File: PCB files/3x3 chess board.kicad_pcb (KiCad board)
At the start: 2 copper layers, 189 x 115.1 mm, 81 parts, among them J1 Conn_01x03, J10 Conn_01x02, J11 USB4216-03-A_REVA, J12 Conn_01x03, J2 Conn_01x03, J4 Conn_01x03, J5 Conn_01x03, J6 Conn_01x03, J7 Conn_01x03, J8 Conn_01x03, J9 Conn_01x03, U1 MCP23S17_SO, U2 MCP23S17_SO, U3 W25Q128JVS, U4 RP2040, X1 ABM8-272-T3

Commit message: update
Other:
- board size 189 x 115.1 mm -> 125.3 x 114.6 mm
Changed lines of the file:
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@@
 	(gr_line
 		(start 49.74 44.25)
-		(end 238.77 43.53)
+		(end 175.04 43.84)
 		(stroke
 			(width 0.05)
@@
 	)
 	(gr_line
-		(start 237.78 158.62)
+		(start 174.864772 158.48945)
 		(end 49.83 158.23)
 		(stroke
@@
 		(polygon
 			(pts
-				(xy 49 47) (xy 49 160) (xy 237 160) (xy 238.032967 158.967033) (xy 238.032967 45) (xy 51 45)
+				(xy 49 47) (xy 49 160) (xy 174.56 159.18) (xy 175.582967 159.204287) (xy 175.582967 45) (xy 51 45)
 			)
 		)
@@
 		(polygon
 			(pts
-				(xy 238 157) (xy 49 161) (xy 49 45) (xy 239 45) (xy 239 41) (xy 239 46)
+				(xy 175.58 158.77) (xy 49 161) (xy 49 45) (xy 174.26 45.06) (xy 174.86 45.36) (xy 175.35 45.18)
 			)
 		)

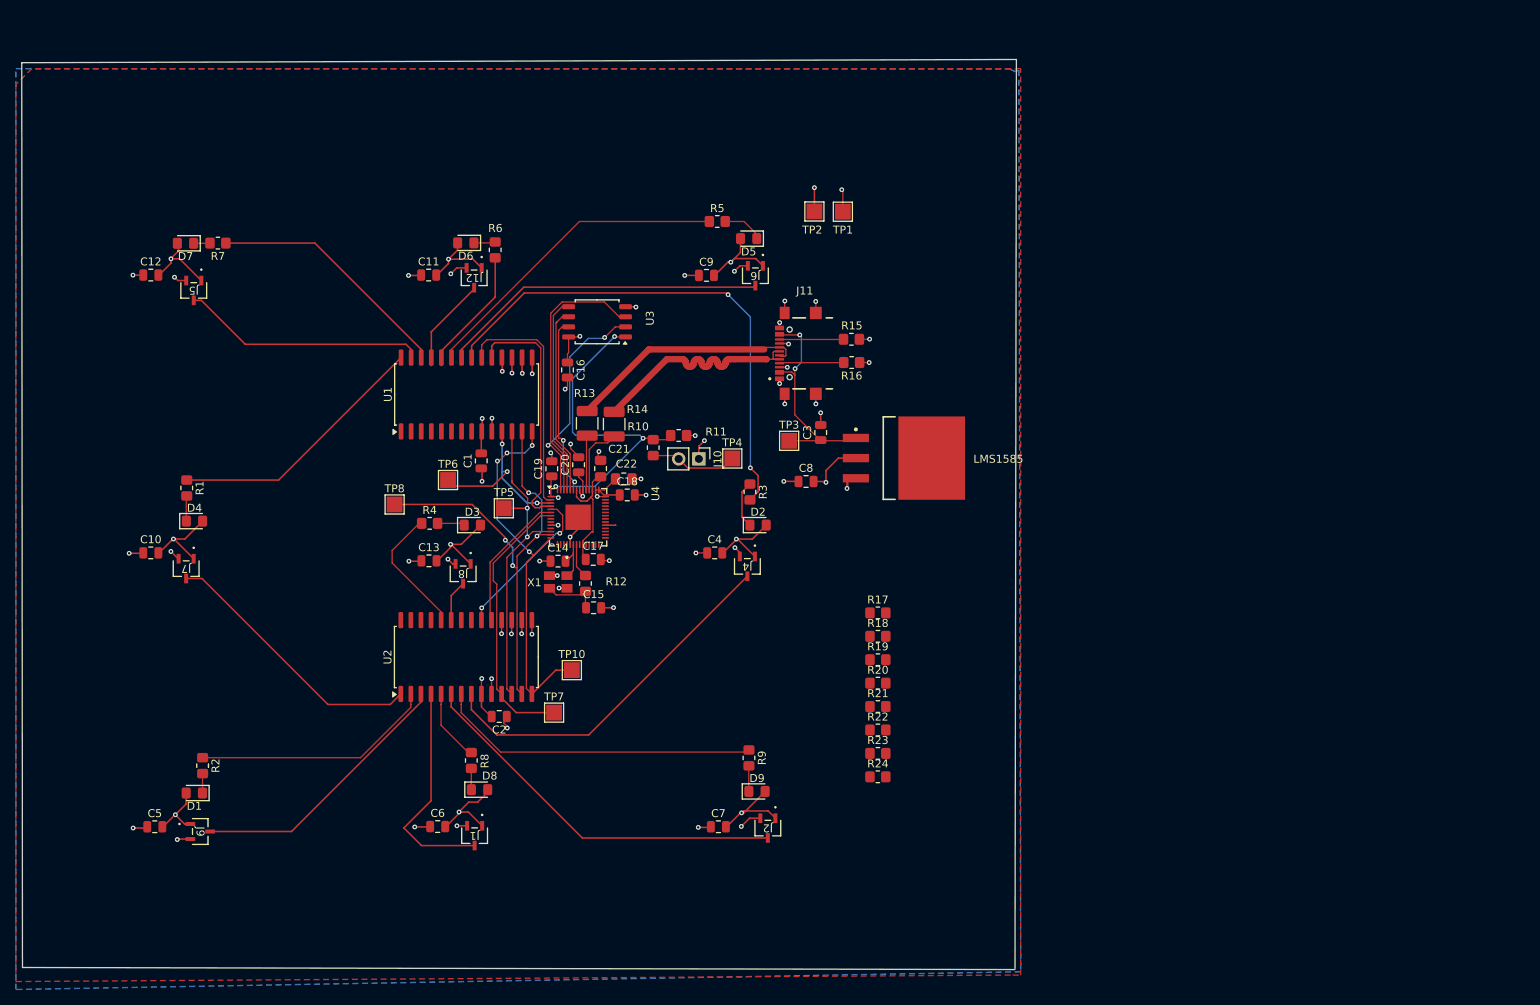
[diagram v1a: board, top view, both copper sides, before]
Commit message: update schematic and and pcb w/ new mcu
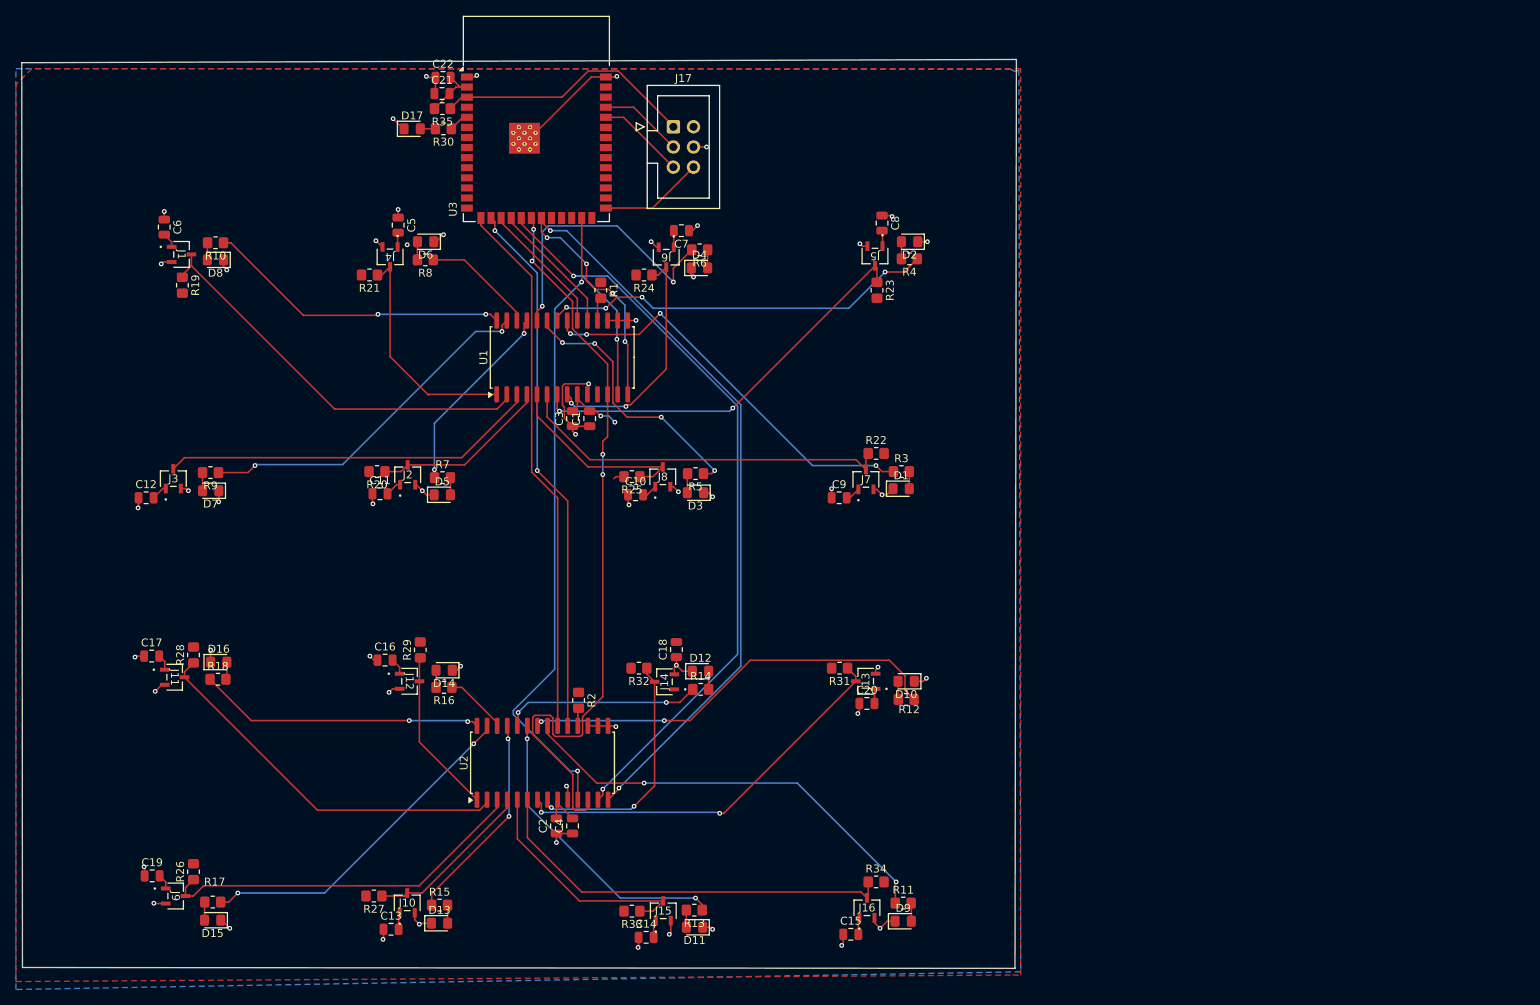
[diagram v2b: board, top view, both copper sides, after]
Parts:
- removed LMS1585: ~, LMS1585:KTT0003B
- removed TP1, TP10, TP3, TP4, TP5, TP6, TP7, TP8: TestPoint, TestPoint:TestPoint_Pad_2.0x2.0mm
- removed TP2: Ground test point, TestPoint:TestPoint_Pad_2.0x2.0mm
- removed U4: RP2040, Package_DFN_QFN:QFN-56-1EP_7x7mm_P0.4mm_EP3.2x3.2mm
- removed X1: ABM8-272-T3, ABM8 - 272 - T3:ABM8-272-T3_ABR
- added D10: LED, Diode_SMD:D_0805_2012Metric_Pad1.15x1.40mm_HandSolder, F.Cu at (161.2, 122.2)
- added D11: LED, Diode_SMD:D_0805_2012Metric_Pad1.15x1.40mm_HandSolder, F.Cu at (134.5, 153.2)
- added D12: LED, Diode_SMD:D_0805_2012Metric_Pad1.15x1.40mm_HandSolder, F.Cu at (135.2, 120.9)
- added D13: LED, Diode_SMD:D_0805_2012Metric_Pad1.15x1.40mm_HandSolder, F.Cu at (102.4, 152.7)
- added D14: LED, Diode_SMD:D_0805_2012Metric_Pad1.15x1.40mm_HandSolder, F.Cu at (103.0, 120.8)
- added D15: LED, Diode_SMD:D_0805_2012Metric_Pad1.15x1.40mm_HandSolder, F.Cu at (73.8, 152.3)
- added D16: LED, Diode_SMD:D_0805_2012Metric_Pad1.15x1.40mm_HandSolder, F.Cu at (74.6, 119.8)
- added D17: LED, Diode_SMD:D_0805_2012Metric_Pad1.15x1.40mm_HandSolder, F.Cu at (98.9, 52.6)
- added J13: Conn_01x03, Hall effect sensor:TSOT-3L_MLX92232LSE-AAA-002-SP_MEL, F.Cu at (156.1, 122.2)
- added J14: Conn_01x03, Hall effect sensor:TSOT-3L_MLX92232LSE-AAA-002-SP_MEL, F.Cu at (130.7, 122.2)
- added J15: Conn_01x03, Hall effect sensor:TSOT-3L_MLX92232LSE-AAA-002-SP_MEL, F.Cu at (130.6, 151.1)
- added J16: Conn_01x03, Hall effect sensor:TSOT-3L_MLX92232LSE-AAA-002-SP_MEL, F.Cu at (156.2, 150.7)
- added J17: Conn_02x03_Odd_Even, Connector_IDC:IDC-Header_2x03_P2.54mm_Vertical, F.Cu at (131.8, 52.3)
- added J3: Conn_01x03, Hall effect sensor:TSOT-3L_MLX92232LSE-AAA-002-SP_MEL, F.Cu at (68.8, 96.6)
- added R25: 5k, Resistor_SMD:R_0805_2012Metric_Pad1.20x1.40mm_HandSolder, F.Cu at (126.6, 96.4)
- added R26: 5k, Resistor_SMD:R_0805_2012Metric_Pad1.20x1.40mm_HandSolder, F.Cu at (71.4, 146.2)
- added R27: 5k, Resistor_SMD:R_0805_2012Metric_Pad1.20x1.40mm_HandSolder, F.Cu at (94.1, 149.2)
- added R28: 5k, Resistor_SMD:R_0805_2012Metric_Pad1.20x1.40mm_HandSolder, F.Cu at (71.4, 118.9)
- added R29: 5k, Resistor_SMD:R_0805_2012Metric_Pad1.20x1.40mm_HandSolder, F.Cu at (99.9, 118.2)
- added R30: 320, Resistor_SMD:R_0805_2012Metric_Pad1.20x1.40mm_HandSolder, F.Cu at (102.9, 52.6)
- added R31: 5k, Resistor_SMD:R_0805_2012Metric_Pad1.20x1.40mm_HandSolder, F.Cu at (152.8, 120.5)
- added R32: 5k, Resistor_SMD:R_0805_2012Metric_Pad1.20x1.40mm_HandSolder, F.Cu at (127.5, 120.5)
- added R33: 5k, Resistor_SMD:R_0805_2012Metric_Pad1.20x1.40mm_HandSolder, F.Cu at (126.6, 151.1)
- added R34: 5k, Resistor_SMD:R_0805_2012Metric_Pad1.20x1.40mm_HandSolder, F.Cu at (157.4, 147.4)
- added R35: 5k, Resistor_SMD:R_0805_2012Metric_Pad1.20x1.40mm_HandSolder, F.Cu at (102.7, 50.0)
- C14, C15: value 15pF -> 10nF
- C16, C17, C18, C19, C20: value 0.1uF -> 10nF
- C21: footprint Capacitor_SMD:C_0805_2012Metric_Pad1.18x1.45mm_HandSolder -> Capacitor_SMD:C_0805_2012Metric
- C22: value 1uF -> 0.1uF; footprint Capacitor_SMD:C_0805_2012Metric_Pad1.18x1.45mm_HandSolder -> Capacitor_SMD:C_0805_2012Metric
- C3: value 10uF -> 1uF
- C4: value 10nF -> 1uF
- C8: value 10uF -> 10nF
- J10: value Conn_01x02 -> Conn_01x03; footprint Connector_PinHeader_2.54mm:PinHeader_1x02_P2.54mm_Vertical -> Hall effect sensor:TSOT-3L_MLX92232LSE-AAA-002-SP_MEL
- J11: value USB4216-03-A_REVA -> Conn_01x03; footprint USB receptacle:USB 2.0 -> Hall effect sensor:TSOT-3L_MLX92232LSE-AAA-002-SP_MEL
- R1, R2: value 16 -> 5k
- R10, R12: value 1k -> 16
- R11: value do not fit -> 16
- R13, R14: value 27.4 -> 16; footprint Resistor_SMD:R_1210_3225Metric_Pad1.30x2.65mm_HandSolder -> Resistor_SMD:R_0805_2012Metric_Pad1.20x1.40mm_HandSolder
- R15, R16: value 5.1kΩ -> 16
- R17, R18: value 5k -> 16
- U3: value W25Q128JVS -> ESP32-S3-WROOM-1; footprint Package_SO:SOIC-8_5.3x5.3mm_P1.27mm -> RF_Module:ESP32-S3-WROOM-1
- moved R19 99.5 mm to (70.0, 72.3), turned to -90 degrees
- moved D1 96.9 mm to (160.5, 97.9), turned to 0 degrees
- moved R17 91.4 mm to (73.8, 150.0), turned to 180 degrees
- moved J11 89.5 mm to (69.0, 121.7), turned to -90 degrees
- moved J7 86.4 mm to (156.1, 96.8), turned to 0 degrees
- moved J5 85.9 mm to (157.2, 68.6)
- moved R15 85.8 mm to (102.4, 150.4)
- moved R21 84.0 mm to (93.5, 71.0), turned to 180 degrees
- moved R18 83.3 mm to (74.5, 121.9)
- moved C6 83.0 mm to (67.7, 65.0), turned to -90 degrees
- moved J1 82.0 mm to (69.9, 68.4), turned to -90 degrees
- moved C5 81.8 mm to (97.2, 64.7), turned to -90 degrees
- moved R9 76.8 mm to (73.5, 95.9), turned to 180 degrees
- moved C7 75.2 mm to (132.8, 65.4), turned to 180 degrees
- moved D8 74.6 mm to (74.1, 69.1), turned to 180 degrees
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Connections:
- C14 pad 2: /XIN -> +3.3V
- C15 pad 1: Net-(C15-Pad1) -> GND
- C15 pad 2: GND -> +3.3V
- C16 pad 1: +3.3V -> GND
- C16 pad 2: GND -> +3.3V
- C17 pad 1: +1V1 -> GND
- C17 pad 2: GND -> +3.3V
- C18 pad 1: +3.3V -> GND
- C18 pad 2: GND -> +3.3V
- C19 pad 1: +3.3V -> GND
- C19 pad 2: GND -> +3.3V
- C20 pad 1: +3.3V -> GND
- C20 pad 2: GND -> +3.3V
- C21 pad 1: +1V1 -> GND
- C21 pad 2: GND -> +3.3V
- C22 pad 1: +3.3V -> GND
- C22 pad 2: GND -> +3.3V
- C3 pad 1: VBUS -> GND
- C3 pad 2: GND -> +3.3V
- C8 pad 1: +3.3V -> GND
- C8 pad 2: GND -> +3.3V
- D1 pad 1: Net-(D1-K) -> GND
- D1 pad 2: +3.3V -> Net-(D1-A)
- D2 pad 1: Net-(D2-K) -> GND
- D2 pad 2: +3.3V -> Net-(D2-A)
- D3 pad 1: Net-(D3-K) -> GND
- D3 pad 2: +3.3V -> Net-(D3-A)
- D4 pad 1: Net-(D4-K) -> GND
- D4 pad 2: +3.3V -> Net-(D4-A)
- D5 pad 1: Net-(D5-K) -> GND
- D5 pad 2: +3.3V -> Net-(D5-A)
- D6 pad 1: Net-(D6-K) -> GND
- D6 pad 2: +3.3V -> Net-(D6-A)
- D7 pad 1: Net-(D7-K) -> GND
- D7 pad 2: +3.3V -> Net-(D7-A)
- D8 pad 1: Net-(D8-K) -> GND
- D8 pad 2: +3.3V -> Net-(D8-A)
- D9 pad 1: Net-(D9-K) -> GND
- D9 pad 2: +3.3V -> Net-(D9-A)
- J1 pad 3: /HALL8 -> /HALL2
- J10 pad 1: GND -> +3.3V
- J10 pad 2: Net-(J10-Pin_2) -> GND
- J12 pad 3: /HALL1 -> /HALL9
- J2 pad 3: /HALL9 -> /HALL4
- J4 pad 3: /HALL6 -> /HALL1
- J5 pad 3: /HALL2 -> /HALL7
- J6 pad 3: /HALL3 -> /HALL8
- J7 pad 3: /HALL4 -> /HALL6
- J9 pad 3: /HALL7 -> /HALL11
- R1 pad 1: Net-(U1-GPA7) -> +3.3V
- R1 pad 2: Net-(D4-K) -> Net-(U1-~{RESET})
- R10 pad 1: Net-(J10-Pin_2) -> Net-(U1-GPA7)
- R10 pad 2: /CS_{flash} -> Net-(D8-A)
- R11 pad 1: +3.3V -> Net-(U2-GPA0)
- R11 pad 2: /CS_{flash} -> Net-(D9-A)
- R12 pad 1: Net-(C15-Pad1) -> Net-(U2-GPA1)
- R12 pad 2: /XOUT -> Net-(D10-A)
- R13 pad 1: /D+ -> Net-(U2-GPA2)
- R14 pad 1: /D- -> Net-(U2-GPA3)
- R15 pad 1: Net-(J11-CC1) -> Net-(U2-GPA4)
- R15 pad 2: GND -> Net-(D13-A)
- R16 pad 1: Net-(J11-CC2) -> Net-(U2-GPA5)
- R16 pad 2: GND -> Net-(D14-A)
- R17 pad 1: /HALL1 -> Net-(U2-GPA6)
- R17 pad 2: +3.3V -> Net-(D15-A)
- R18 pad 1: /HALL2 -> Net-(U2-GPA7)
- R18 pad 2: +3.3V -> Net-(D16-A)
- R19 pad 1: /HALL6 -> /HALL2
- R2 pad 1: Net-(U2-GPB1) -> +3.3V
- R2 pad 2: Net-(D1-K) -> Net-(U2-~{RESET})
- R20 pad 1: /HALL7 -> /HALL4
- R21 pad 1: /HALL8 -> /HALL1
- R22 pad 1: /HALL4 -> /HALL6
- R23 pad 1: /HALL5 -> /HALL7
- R24 pad 1: /HALL9 -> /HALL8
- R3 pad 1: Net-(D2-K) -> Net-(U1-GPA0)
- R3 pad 2: Net-(U1-GPA0) -> Net-(D1-A)
- R4 pad 1: Net-(U2-GPA3) -> Net-(U1-GPA1)
- R4 pad 2: Net-(D3-K) -> Net-(D2-A)
- R5 pad 2: Net-(D5-K) -> Net-(D3-A)
- R6 pad 1: Net-(U1-GPA3) -> Net-(D4-A)
- R6 pad 2: Net-(D6-K) -> Net-(U1-GPA3)
- R7 pad 1: Net-(U1-GPA5) -> Net-(U1-GPA4)
- R7 pad 2: Net-(D7-K) -> Net-(D5-A)
- R8 pad 1: Net-(U2-GPB4) -> Net-(U1-GPA5)
- R8 pad 2: Net-(D8-K) -> Net-(D6-A)
- R9 pad 1: Net-(U2-GPB6) -> Net-(U1-GPA6)
- R9 pad 2: Net-(D9-K) -> Net-(D7-A)
- U1 pad 1: unconnected-(U1-GPB0-Pad1) -> /HALL1
- U1 pad 11: /CS_{extender1} -> unconnected-(U1-~{CS}-Pad11)
- U1 pad 18: +3.3V -> Net-(U1-~{RESET})
- U1 pad 2: unconnected-(U1-GPB1-Pad2) -> /HALL2
- U1 pad 22: /HALL3 -> Net-(U1-GPA1)
- U1 pad 25: /HALL1 -> Net-(U1-GPA4)
- U1 pad 27: /HALL2 -> Net-(U1-GPA6)
- U1 pad 3: unconnected-(U1-GPB2-Pad3) -> /HALL3
- U1 pad 4: unconnected-(U1-GPB3-Pad4) -> /HALL4
- U1 pad 5: unconnected-(U1-GPB4-Pad5) -> /HALL5
- U1 pad 6: unconnected-(U1-GPB5-Pad6) -> /HALL6
- U1 pad 7: unconnected-(U1-GPB6-Pad7) -> /HALL7
- U1 pad 8: unconnected-(U1-GPB7-Pad8) -> /HALL8
- U2 pad 1: /HALL4 -> /HALL9
- U2 pad 18: +3.3V -> Net-(U2-~{RESET})
- U2 pad 2: Net-(U2-GPB1) -> /HALL10
- U2 pad 21: unconnected-(U2-GPA0-Pad21) -> Net-(U2-GPA0)
- U2 pad 22: unconnected-(U2-GPA1-Pad22) -> Net-(U2-GPA1)
- U2 pad 23: /HALL5 -> Net-(U2-GPA2)
- U2 pad 25: unconnected-(U2-GPA4-Pad25) -> Net-(U2-GPA4)
- U2 pad 26: unconnected-(U2-GPA5-Pad26) -> Net-(U2-GPA5)
- U2 pad 27: unconnected-(U2-GPA6-Pad27) -> Net-(U2-GPA6)
- U2 pad 28: unconnected-(U2-GPA7-Pad28) -> Net-(U2-GPA7)
- U2 pad 3: /HALL7 -> /HALL11
- U2 pad 4: /HALL8 -> /HALL12
- U2 pad 5: Net-(U2-GPB4) -> /HALL13
- U2 pad 6: /HALL9 -> /HALL14
- U2 pad 7: Net-(U2-GPB6) -> /HALL15
- U2 pad 8: /HALL6 -> /HALL16
- U3 pad 1: /CS_{flash} -> GND
- U3 pad 2: /SD2 -> +3.3V
- U3 pad 3: /SD3 -> /EN
- U3 pad 4: GND -> unconnected-(U3-IO4-Pad4)
- U3 pad 5: /SD1 -> /LED_test
- U3 pad 6: /QSCLK -> unconnected-(U3-IO6-Pad6)
- U3 pad 7: /SD4 -> unconnected-(U3-IO7-Pad7)
- U3 pad 8: +3.3V -> unconnected-(U3-IO15-Pad8)
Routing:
- net +3.3V: track 139.4 -> 54.0 mm, vias 22 -> 2
- net /MISO: track 48.3 -> 120.5 mm, vias 4 -> 6
- net Net-(U2-GPA0): track 0.00 -> 55.4 mm, vias 0 -> 2
- net /SCK: track 41.6 -> 96.0 mm, vias 2 -> 4
- net /MOSI: track 58.1 -> 112.3 mm, vias 4 -> 3
- net Net-(U2-GPA1): track 0.00 -> 54.0 mm, vias 0 -> 2
- net /HALL14: track 0.00 -> 52.8 mm
- net /HALL15: track 0.00 -> 50.5 mm, vias 0 -> 2
- net /INTB_{extender2}: track 17.6 -> 68.0 mm, vias 0 -> 2
- net Net-(U1-GPA1): track 0.00 -> 50.1 mm, vias 0 -> 4
- net /INTA_{extender2}: track 19.5 -> 68.0 mm, vias 2 -> 0
- net /HALL10: track 0.00 -> 48.1 mm
- net /HALL11: track 0.00 -> 47.4 mm
- net /CS_{extender2}: track 34.5 -> 80.8 mm, vias 0 -> 2
- net Net-(U1-GPA6): track 0.00 -> 44.7 mm, vias 0 -> 2
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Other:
- board size 125.3 x 114.6 mm -> 125.3 x 114.5 mm
- board text added: "MCP23S17_SO"

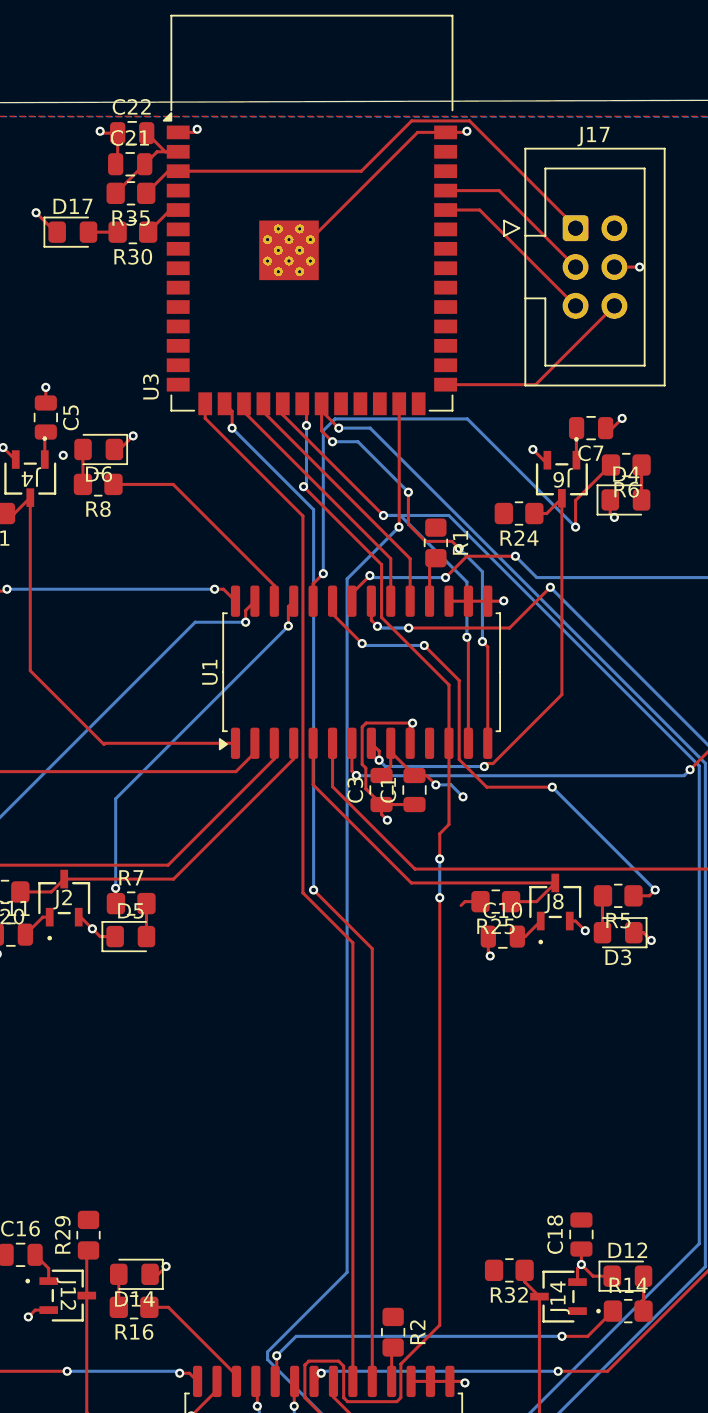
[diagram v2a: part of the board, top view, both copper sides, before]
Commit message: Changes
- updated PCB
- now pieces can't move such that check is allowed
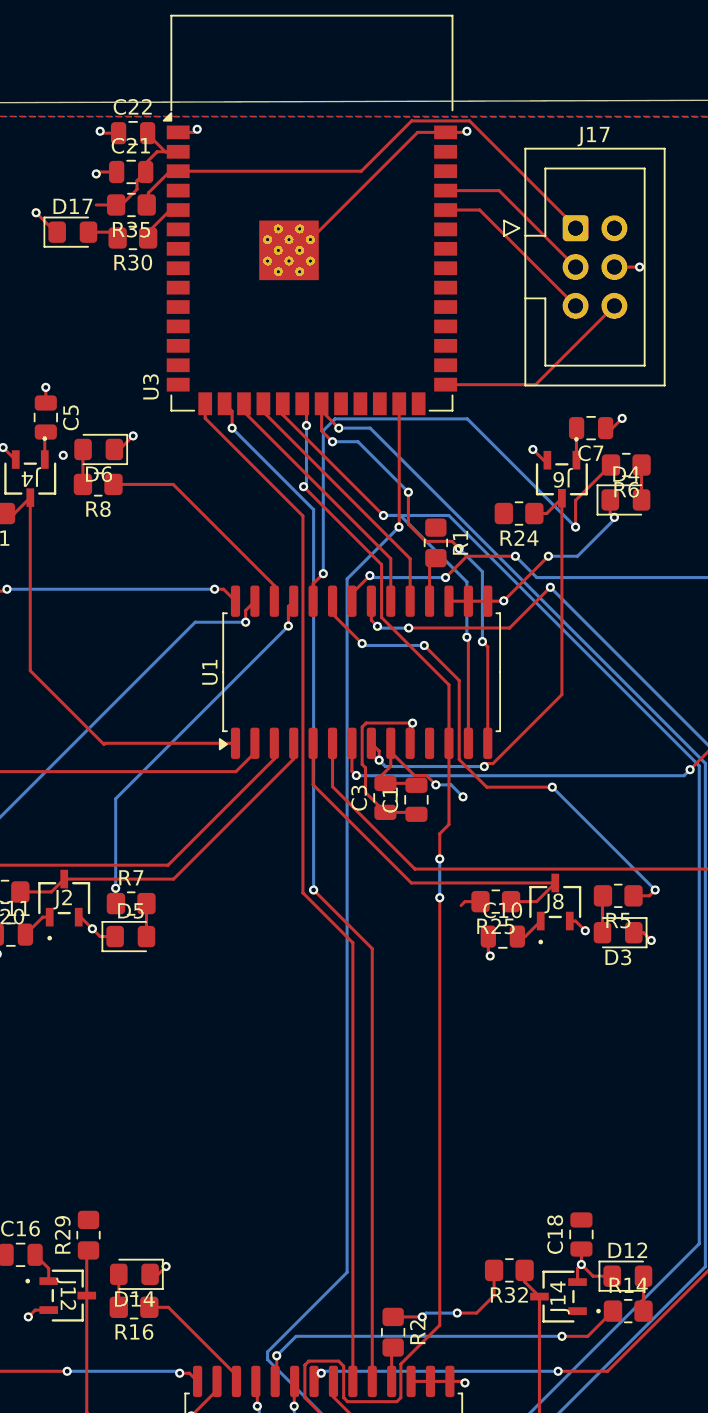
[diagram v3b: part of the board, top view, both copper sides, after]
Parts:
- moved R35 0.76 mm to (102.8, 50.8)
- moved C1 0.65 mm to (121.4, 89.7)
- moved C3 0.57 mm to (119.4, 89.6)
- moved C21 0.51 mm to (102.7, 48.6)
- moved R30 0.38 mm to (102.9, 53.0)
- moved C22 0.06 mm to (102.9, 46.1)
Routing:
- net +3.3V: track 54.0 -> 66.9 mm, vias 2 -> 4
- net GND: track 115.6 -> 124.0 mm, vias 54 -> 55
- net /EN: track 33.1 -> 34.3 mm
